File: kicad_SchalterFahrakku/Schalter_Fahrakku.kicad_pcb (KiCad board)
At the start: 2 copper layers, 55 x 25 mm, 31 parts, among them P1 V_IN+, P2 V_IN-, P3 uC_IN, P4 V_OUT+, P5 V_OUT-, Q1 IRLML6344, Q2 IPD90P03

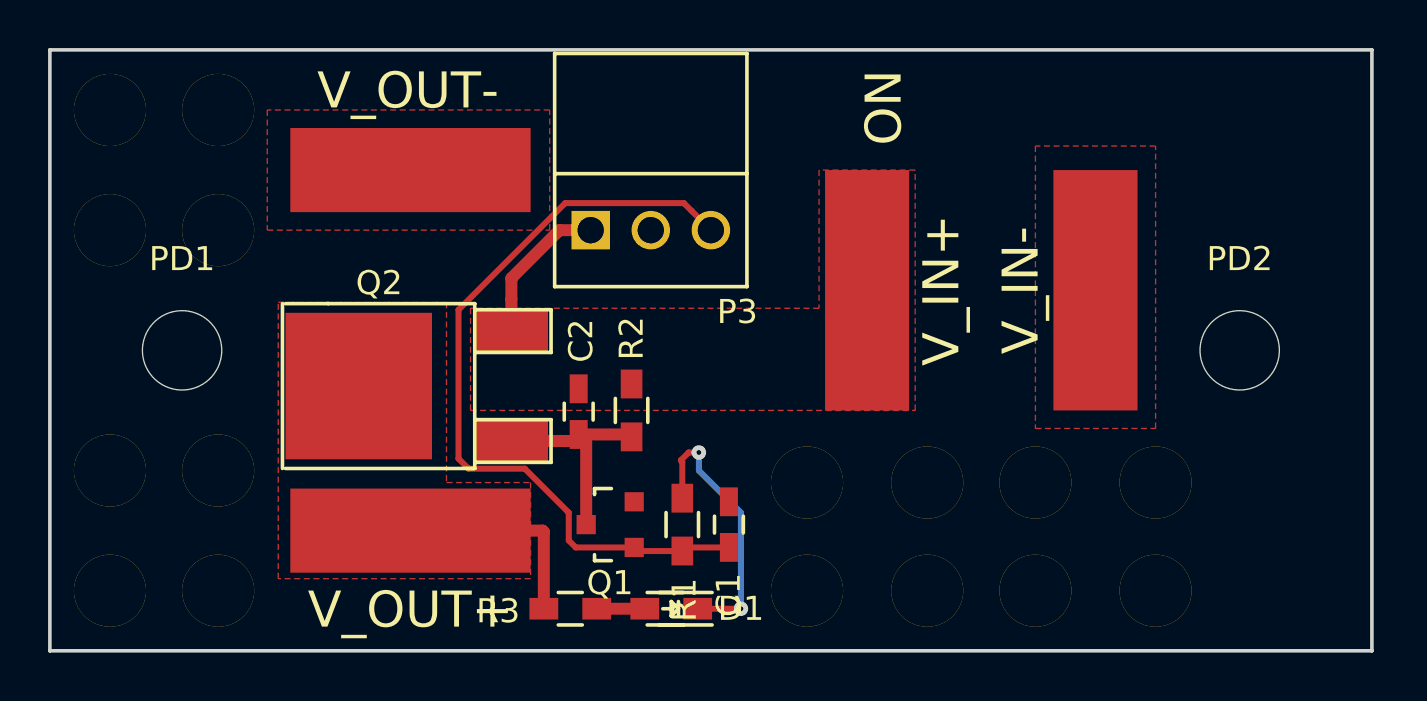
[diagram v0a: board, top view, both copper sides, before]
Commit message: - Sperrflächen verschoben
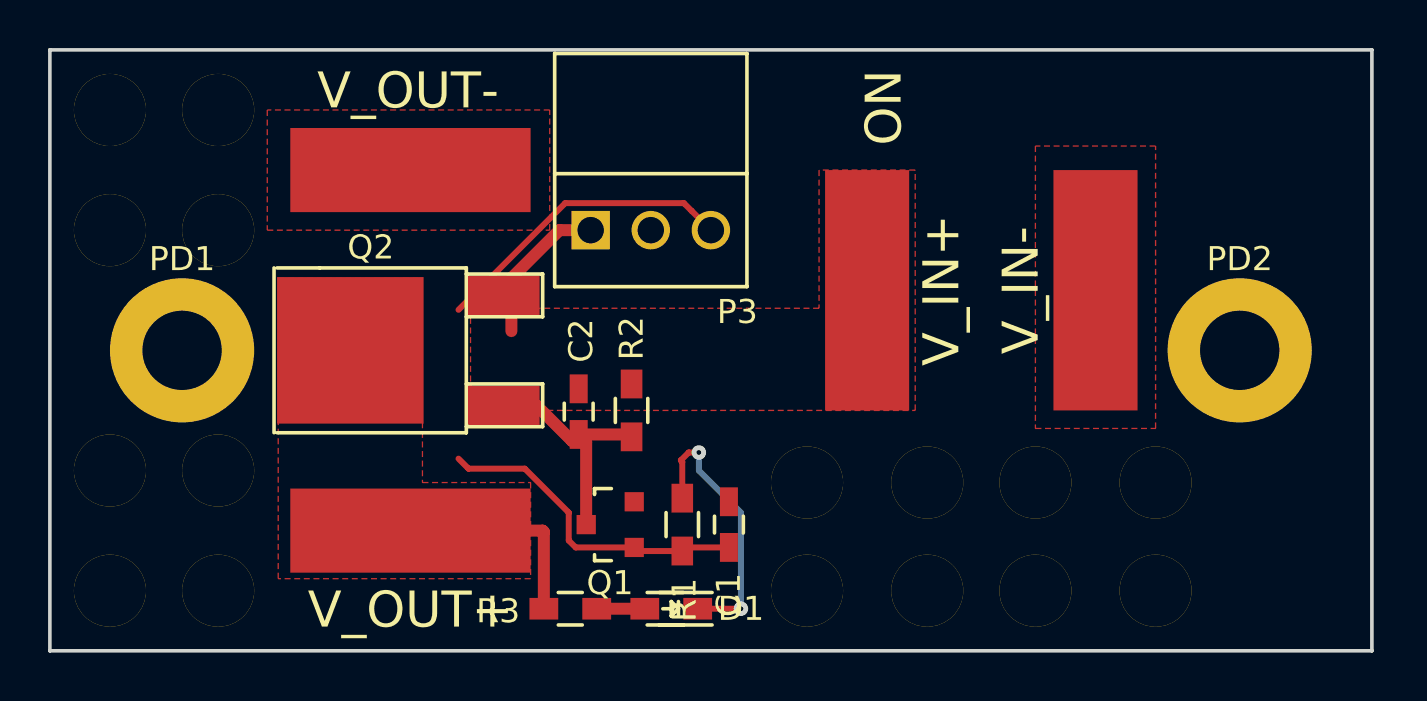
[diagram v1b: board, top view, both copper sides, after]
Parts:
- moved Q2 1.53 mm to (118.8, 82.5)
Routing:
- net /CTL_DRIVE: track 32.6 -> 26.4 mm
- net Net-(C2-Pad2): track 9.03 -> 10.00 mm
- net Net-(C2-Pad1): track 6.33 -> 5.45 mm
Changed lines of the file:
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@@
     (thickness 1.6)
     (drawings 11)
-    (tracks 40)
+    (tracks 39)
     (zones 0)
     (modules 31)
@@
   )
   (setup
-    (last_trace_width 0.25)
+    (last_trace_width 0.3)
     (user_trace_width 0.2)
     (user_trace_width 0.25)
@@
   )
   (module TO_SOT_Packages_SMD:TO-252-2Lead (layer F.Cu)
-    (at 119.2 83.986 90)
+    (at 118.85 82.5 90)
     (descr "DPAK / TO-252 2-lead smd package")
     (tags "dpak TO-252")
@@
     )
   )
-  (module Custom:MountingHole_3.3mm_M3 (layer F.Cu)
-    (at 105.5 82.5)
-    (descr "Mounting Hole 3.3mm")
-    (tags "mounting hole 3.3mm")
-    (fp_text reference PD1 (at 0 -3.8) (layer F.SilkS)
-      (effects (font (size 1 1) (thickness 0.15)))
-    )
-    (fp_text value Hole (at 0 3.8) (layer F.Fab)
-      (effects (font (size 1 1) (thickness 0.15)))
-    )
-    (fp_circle (center 0 0) (end 2.8 0) (layer Cmts.User) (width 0.15))
-    (fp_circle (center 0 0) (end 3.05 0) (layer F.CrtYd) (width 0.05))
-    (pad "" np_thru_hole circle (at 0 0) (size 3.3 3.3) (drill 3.3) (layers *.Cu *.Mask F.SilkS))
-  )
-  (module Custom:MountingHole_3.3mm_M3 (layer F.Cu)
-    (at 149.5 82.5)
-    (descr "Mounting Hole 3.3mm")
-    (tags "mounting hole 3.3mm")
-    (fp_text reference PD2 (at 0 -3.8) (layer F.SilkS)
-      (effects (font (size 1 1) (thickness 0.15)))
-    )
-    (fp_text value Hole (at 0 3.8) (layer F.Fab)
-      (effects (font (size 1 1) (thickness 0.15)))
-    )
-    (fp_circle (center 0 0) (end 2.8 0) (layer Cmts.User) (width 0.15))
-    (fp_circle (center 0 0) (end 3.05 0) (layer F.CrtYd) (width 0.05))
-    (pad "" np_thru_hole circle (at 0 0) (size 3.3 3.3) (drill 3.3) (layers *.Cu *.Mask F.SilkS))
-  )
   (module Custom:LED_0603_HandSoldering (layer F.Cu)
     (at 125.85 93.25 180)
@@
     (pad 1 thru_hole circle (at 0 0) (size 3 3) (drill 3) (layers *.Cu *.Mask F.SilkS))
   )
+  (module Custom:MountingHole_3.3mm_M3 (layer F.Cu)
+    (at 105.5 82.5)
+    (descr "Mounting Hole 3.3mm")
+    (tags "mounting hole 3.3mm")
+    (fp_text reference PD1 (at 0 -3.8) (layer F.SilkS)
+      (effects (font (size 1 1) (thickness 0.15)))
+    )
+    (fp_text value Hole (at 0 3.8) (layer F.Fab)
+      (effects (font (size 1 1) (thickness 0.15)))
+    )
+    (fp_circle (center 0 0) (end 2.8 0) (layer Cmts.User) (width 0.15))
+    (fp_circle (center 0 0) (end 3.05 0) (layer F.CrtYd) (width 0.05))
+    (pad "" np_thru_hole circle (at 0 0) (size 6 6) (drill 3.3) (layers *.Cu *.Mask F.SilkS))
+  )
+  (module Custom:MountingHole_3.3mm_M3 (layer F.Cu)
+    (at 149.5 82.5)
+    (descr "Mounting Hole 3.3mm")
+    (tags "mounting hole 3.3mm")
+    (fp_text reference PD2 (at 0 -3.8) (layer F.SilkS)
+      (effects (font (size 1 1) (thickness 0.15)))
+    )
+    (fp_text value Hole (at 0 3.8) (layer F.Fab)
+      (effects (font (size 1 1) (thickness 0.15)))
+    )
+    (fp_circle (center 0 0) (end 2.8 0) (layer Cmts.User) (width 0.15))
+    (fp_circle (center 0 0) (end 3.05 0) (layer F.CrtYd) (width 0.05))
+    (pad "" np_thru_hole circle (at 0 0) (size 6 6) (drill 3.3) (layers *.Cu *.Mask F.SilkS))
+  )
   (gr_text "ON\n" (at 134.7 72.4 90) (layer F.SilkS)
     (effects (font (size 1.5 1.5) (thickness 0.3)))
@@
   (gr_line (start 100 95) (end 155 95) (layer Edge.Cuts) (width 0.15))
   (gr_line (start 100 70) (end 100 95) (layer Edge.Cuts) (width 0.15))
-  (segment (start 117 87.006502) (end 117 80.814998) (width 0.25) (layer F.Cu) (net 1))
   (segment (start 117 80.814998) (end 121.439999 76.374999) (width 0.25) (layer F.Cu) (net 1))
   (segment (start 121.439999 76.374999) (end 126.374999 76.374999) (width 0.25) (layer F.Cu) (net 1))
@@
   (segment (start 122.5 77.5) (end 121.2 77.5) (width 0.5) (layer F.Cu) (net 3))
   (segment (start 121.2 77.5) (end 119.2 79.5) (width 0.5) (layer F.Cu) (net 3))
-  (segment (start 119.2 79.5) (end 119.2 80.3745) (width 0.5) (layer F.Cu) (net 3))
   (segment (start 119.2 80.3745) (end 119.2 81.7) (width 0.5) (layer F.Cu) (net 3))
+  (segment (start 118.85 84.786) (end 120.242 84.786) (width 0.5) (layer F.Cu) (net 4))
+  (segment (start 120.242 84.786) (end 121.728 86.272) (width 0.5) (layer F.Cu) (net 4))
   (segment (start 122 86) (end 124.1 86) (width 0.5) (layer F.Cu) (net 4))
   (segment (start 124.1 86) (end 124.2 86.1) (width 0.5) (layer F.Cu) (net 4))
-  (segment (start 119.2 86.272) (end 121.728 86.272) (width 0.5) (layer F.Cu) (net 4))
   (segment (start 121.728 86.272) (end 122 86) (width 0.5) (layer F.Cu) (net 4))
   (segment (start 122.31178 89.75) (end 122.31178 86.31178) (width 0.5) (layer F.Cu) (net 4))
@@
     (polygon
       (pts
-        (xy 116.5 88) (xy 120 88) (xy 120 92) (xy 109.5 92) (xy 109.5 80.5)
-        (xy 116.5 80.5) (xy 116.5 88)
+        (xy 115.5 88) (xy 120 88) (xy 120 92) (xy 109.5 92) (xy 109.5 79.5)
+        (xy 115.5 79.5) (xy 115.5 88)
       )
     )

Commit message: - Versorgungsspannung verbunden - Lötjumper für MPU_INT vorgesehen
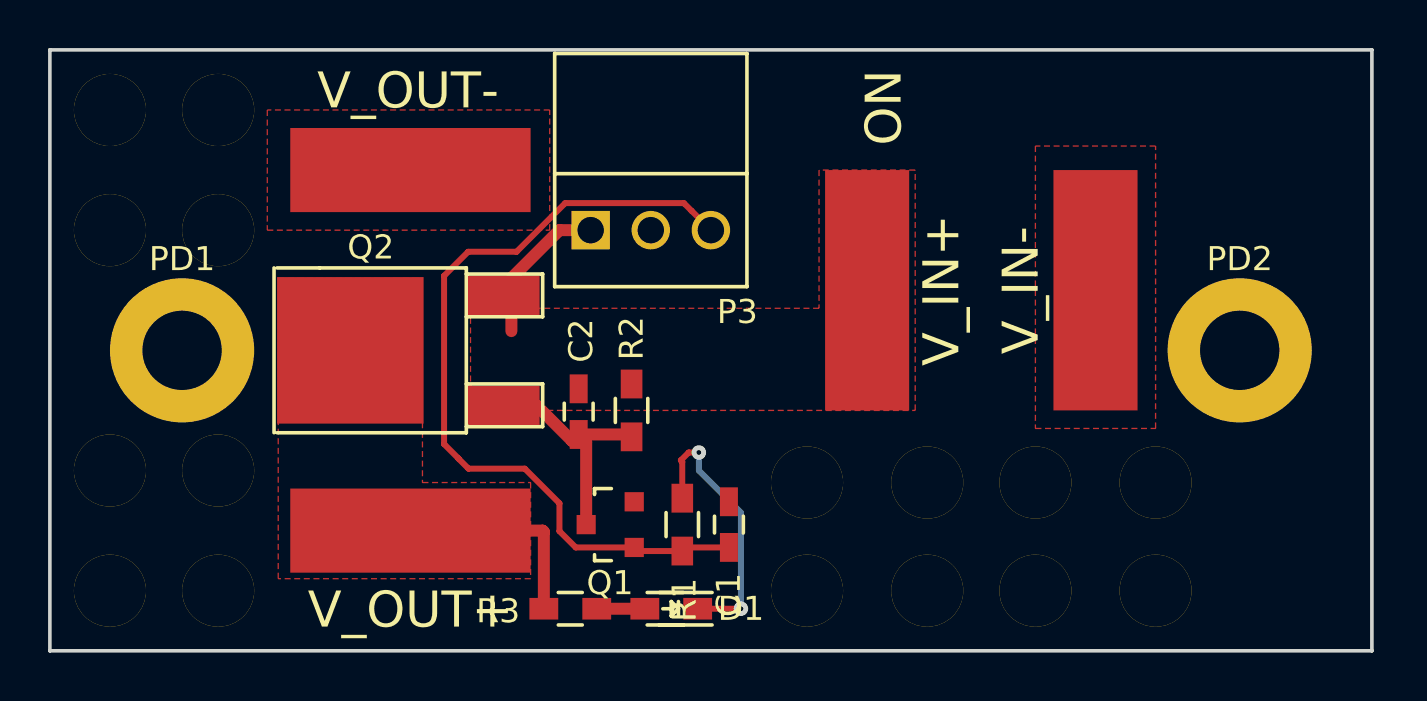
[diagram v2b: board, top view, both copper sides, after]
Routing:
- net /CTL_DRIVE: track 26.4 -> 34.3 mm
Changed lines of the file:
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@@
     (thickness 1.6)
     (drawings 11)
-    (tracks 39)
+    (tracks 44)
     (zones 0)
     (modules 31)
@@
   )
   (setup
-    (last_trace_width 0.3)
+    (last_trace_width 0.25)
     (user_trace_width 0.2)
     (user_trace_width 0.25)
@@
   (gr_line (start 100 95) (end 155 95) (layer Edge.Cuts) (width 0.15))
   (gr_line (start 100 70) (end 100 95) (layer Edge.Cuts) (width 0.15))
-  (segment (start 117 80.814998) (end 121.439999 76.374999) (width 0.25) (layer F.Cu) (net 1))
+  (segment (start 124.31076 90.7) (end 121.876678 90.7) (width 0.25) (layer F.Cu) (net 1))
+  (segment (start 116.4 79.4) (end 117.4 78.4) (width 0.25) (layer F.Cu) (net 1))
+  (segment (start 121.876678 90.7) (end 121.2 90.023322) (width 0.25) (layer F.Cu) (net 1))
+  (segment (start 117 87) (end 116.4 86.4) (width 0.25) (layer F.Cu) (net 1))
+  (segment (start 121.2 90.023322) (end 121.2 88.864998) (width 0.25) (layer F.Cu) (net 1))
+  (segment (start 117.415999 87.422501) (end 117 87.006502) (width 0.25) (layer F.Cu) (net 1))
+  (segment (start 117.4 78.4) (end 119.414998 78.4) (width 0.25) (layer F.Cu) (net 1))
+  (segment (start 121.2 88.864998) (end 119.757503 87.422501) (width 0.25) (layer F.Cu) (net 1))
+  (segment (start 119.757503 87.422501) (end 117.415999 87.422501) (width 0.25) (layer F.Cu) (net 1))
+  (segment (start 117 87.006502) (end 117 87) (width 0.25) (layer F.Cu) (net 1))
+  (segment (start 116.4 86.4) (end 116.4 79.4) (width 0.25) (layer F.Cu) (net 1))
   (segment (start 121.439999 76.374999) (end 126.374999 76.374999) (width 0.25) (layer F.Cu) (net 1))
+  (segment (start 119.414998 78.4) (end 121.439999 76.374999) (width 0.25) (layer F.Cu) (net 1))
   (segment (start 126.374999 76.374999) (end 126.700001 76.700001) (width 0.25) (layer F.Cu) (net 1))
   (segment (start 126.700001 76.700001) (end 127.5 77.5) (width 0.25) (layer F.Cu) (net 1))
-  (segment (start 124.31076 90.7) (end 121.876678 90.7) (width 0.25) (layer F.Cu) (net 1))
-  (segment (start 121.876678 90.7) (end 121.586729 90.410051) (width 0.25) (layer F.Cu) (net 1))
-  (segment (start 121.586729 90.410051) (end 121.586729 89.251727) (width 0.25) (layer F.Cu) (net 1))
-  (segment (start 121.586729 89.251727) (end 119.757503 87.422501) (width 0.25) (layer F.Cu) (net 1))
-  (segment (start 119.757503 87.422501) (end 117.415999 87.422501) (width 0.25) (layer F.Cu) (net 1))
-  (segment (start 117.415999 87.422501) (end 117 87.006502) (width 0.25) (layer F.Cu) (net 1))
   (segment (start 126.31 90.85) (end 124.46076 90.85) (width 0.25) (layer F.Cu) (net 1))
   (segment (start 124.46076 90.85) (end 124.31076 90.7) (width 0.25) (layer F.Cu) (net 1))

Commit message: - Schalterplatine finalisiert - Beiden Platinen TOP/BOTTOM markierungen hinzugefügt
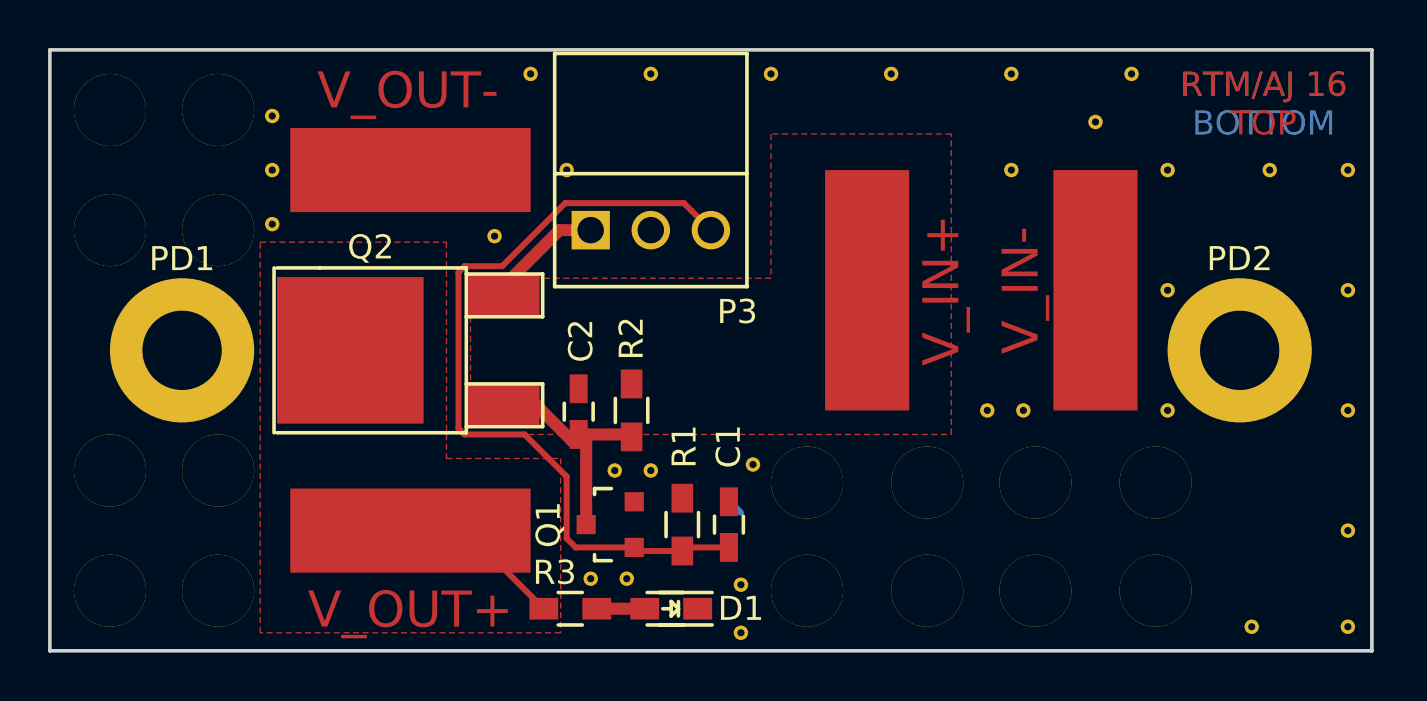
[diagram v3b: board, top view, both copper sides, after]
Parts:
- added REF**: Via_0,6mm, Custom:Via_0,6mm, F.Cu at (150.8, 75.0)
- added REF**: Via_0,6mm, Custom:Via_0,6mm, F.Cu at (143.5, 73.0)
- added REF**: Via_0,6mm, Custom:Via_0,6mm, F.Cu at (146.5, 75.0)
- added REF**: Via_0,6mm, Custom:Via_0,6mm, F.Cu at (146.5, 80.0)
- added REF**: Via_0,6mm, Custom:Via_0,6mm, F.Cu at (146.5, 85.0)
- added REF**: Via_0,6mm, Custom:Via_0,6mm, F.Cu at (140.5, 85.0)
- added REF**: Via_0,6mm, Custom:Via_0,6mm, F.Cu at (139.0, 85.0)
- added REF**: Via_0,6mm, Custom:Via_0,6mm, F.Cu at (150.0, 94.0)
- added REF**: Via_0,6mm, Custom:Via_0,6mm, F.Cu at (154.0, 94.0)
- added REF**: Via_0,6mm, Custom:Via_0,6mm, F.Cu at (154.0, 90.0)
- added REF**: Via_0,6mm, Custom:Via_0,6mm, F.Cu at (154.0, 85.0)
- added REF**: Via_0,6mm, Custom:Via_0,6mm, F.Cu at (121.5, 75.0)
- added REF**: Via_0,6mm, Custom:Via_0,6mm, F.Cu at (154.0, 80.0)
- added REF**: Via_0,6mm, Custom:Via_0,6mm, F.Cu at (154.0, 75.0)
- added REF**: Via_0,6mm, Custom:Via_0,6mm, F.Cu at (123.5, 87.5)
- added REF**: Via_0,6mm, Custom:Via_0,6mm, F.Cu at (125.0, 87.5)
- added REF**: Via_0,6mm, Custom:Via_0,6mm, F.Cu at (129.2, 87.2)
- added REF**: Via_0,6mm, Custom:Via_0,6mm, F.Cu at (128.8, 92.2)
- added REF**: Via_0,6mm, Custom:Via_0,6mm, F.Cu at (128.8, 94.2)
- added REF**: Via_0,6mm, Custom:Via_0,6mm, F.Cu at (145.0, 71.0)
- added REF**: Via_0,6mm, Custom:Via_0,6mm, F.Cu at (118.5, 77.8)
- added REF**: Via_0,6mm, Custom:Via_0,6mm, F.Cu at (109.2, 77.2)
- added REF**: Via_0,6mm, Custom:Via_0,6mm, F.Cu at (109.2, 75.0)
- added REF**: Via_0,6mm, Custom:Via_0,6mm, F.Cu at (109.2, 72.8)
- added REF**: Via_0,6mm, Custom:Via_0,6mm, F.Cu at (124.0, 92.0)
- added REF**: Via_0,6mm, Custom:Via_0,6mm, F.Cu at (122.5, 92.0)
- added REF**: Via_0,6mm, Custom:Via_0,6mm, F.Cu at (140.0, 75.0)
- added REF**11: Via_0,6mm, Custom:Via_0,6mm, F.Cu at (120.0, 71.0)
- added REF**21: Via_0,6mm, Custom:Via_0,6mm, F.Cu at (125.0, 71.0)
- added REF**31: Via_0,6mm, Custom:Via_0,6mm, F.Cu at (130.0, 71.0)
- added REF**41: Via_0,6mm, Custom:Via_0,6mm, F.Cu at (135.0, 71.0)
- added REF**51: Via_0,6mm, Custom:Via_0,6mm, F.Cu at (140.0, 71.0)
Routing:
- net GND: track 11.5 -> 0.71 mm, vias 2 -> 0
- net Net-(P4-Pad1): track 8.77 -> 6.90 mm
- net Net-(C2-Pad1): track 5.45 -> 4.13 mm
- net /CTL_DRIVE: track 34.3 -> 33.6 mm
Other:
- rule pad_to_mask_clearance: 0.2 -> 0.05
- board text added: "RTM/AJ 16 BOTTOM"
- board text added: "RTM/AJ 16 TOP"
- board text removed: "ON"

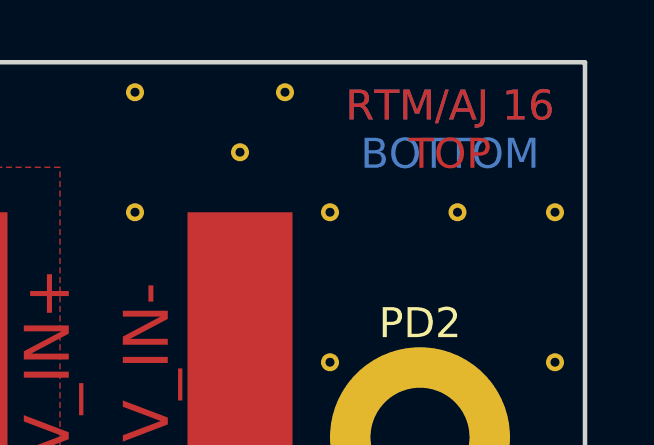
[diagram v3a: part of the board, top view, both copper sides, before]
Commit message: Beschriftungstext auf Unterseite gespiegelt
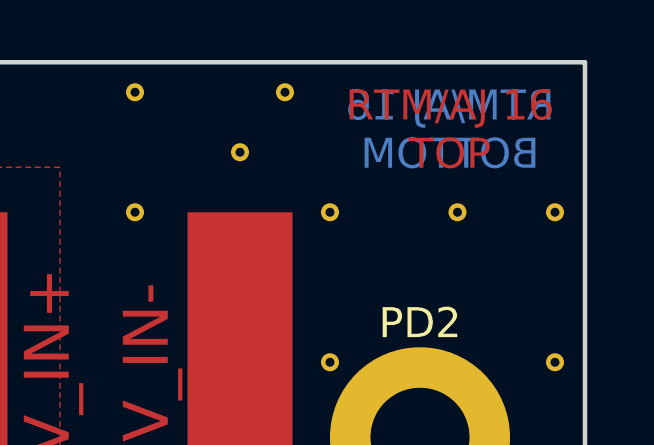
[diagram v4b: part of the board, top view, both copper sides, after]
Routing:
- net GND: track 0.71 -> 0.00 mm
- net (no net): track 0.00 -> 0.71 mm
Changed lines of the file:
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@@
-(kicad_pcb (version 4) (host pcbnew 4.0.2-stable)
+(kicad_pcb (version 4) (host pcbnew 4.0.4-stable)
   (general
-    (links 0)
+    (links 51)
     (no_connects 0)
-    (area 87.000001 69.075 155.075001 115.300001)
+    (area 87.150001 69.225 155.075001 115.300001)
     (thickness 1.6)
     (drawings 13)
@@
   )
   (gr_text "RTM/AJ 16\nBOTTOM" (at 150.5 72.25) (layer B.Cu)
-    (effects (font (size 1 1) (thickness 0.15)))
+    (effects (font (size 1 1) (thickness 0.15)) (justify mirror))
   )
   (gr_text "RTM/AJ 16\nTOP" (at 150.5 72.25) (layer F.Cu)
@@
   (gr_line (start 100 95) (end 155 95) (layer Edge.Cuts) (width 0.15))
   (gr_line (start 100 70) (end 100 95) (layer Edge.Cuts) (width 0.15))
+  (segment (start 128.75 89.25) (end 128.25 88.75) (width 0.25) (layer B.Cu) (net 0))
   (segment (start 124.31076 90.7) (end 121.876678 90.7) (width 0.25) (layer F.Cu) (net 1))
   (segment (start 121.876678 90.7) (end 121.5 90.323322) (width 0.25) (layer F.Cu) (net 1))
@@
   (segment (start 128.25 90.7) (end 126.46 90.7) (width 0.25) (layer F.Cu) (net 1))
   (segment (start 126.46 90.7) (end 126.31 90.85) (width 0.25) (layer F.Cu) (net 1))
-  (segment (start 128.75 89.25) (end 128.25 88.75) (width 0.25) (layer B.Cu) (net 2))
   (segment (start 122.5 77.5) (end 121.2 77.5) (width 0.5) (layer F.Cu) (net 3))
   (segment (start 121.2 77.5) (end 119.2 79.5) (width 0.5) (layer F.Cu) (net 3))
